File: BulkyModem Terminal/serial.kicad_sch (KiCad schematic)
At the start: 12 parts, among them J2 RS-232, J5 TTL, U2 74HCT244, U3 MAX232

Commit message: Part of a layout
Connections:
- net TTL.CTS: now also J5.3 (Pin_3), R21.2; no longer R21.1, U2.11 (2A3)
- net TTL.RTS: now also J5.4 (Pin_4); no longer U2.5 (2Y1)
- net TTL.RxD: now also J5.1 (Pin_1), R15.2; no longer R15.1, U2.13 (2A2)
- net TTL.TxD: now also J5.2 (Pin_2); no longer U2.3 (2Y0)
- net at R16.2: now also U2.5 (2Y1); no longer J5.4 (Pin_4)
- net at R20.2: now also U2.3 (2Y0); no longer J5.2 (Pin_2)
- new net: R15.1, U2.13 (2A2)
- new net: R21.1, U2.11 (2A3)
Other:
- note added: "CTS"
- note added: "RTS"
- note added: "RxD"
- note added: "TxD"
- moved on the sheet: R15

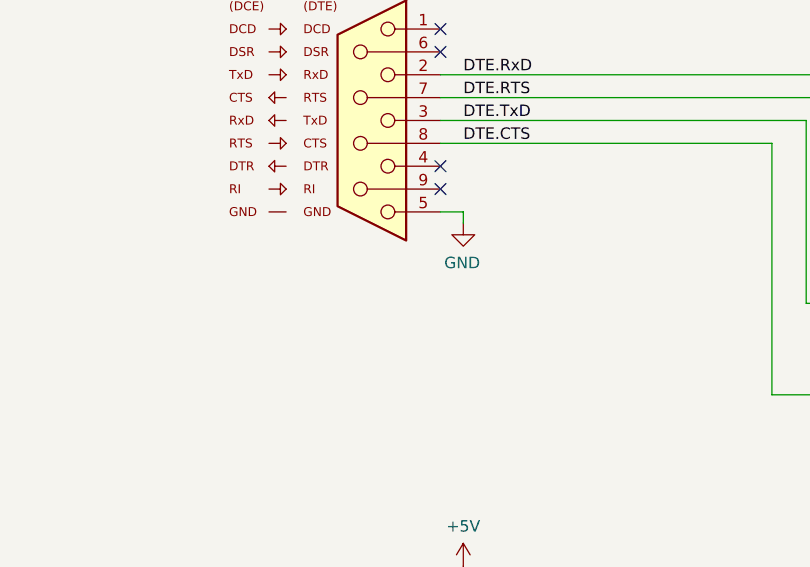
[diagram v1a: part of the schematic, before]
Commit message: Change PS/2 circuit
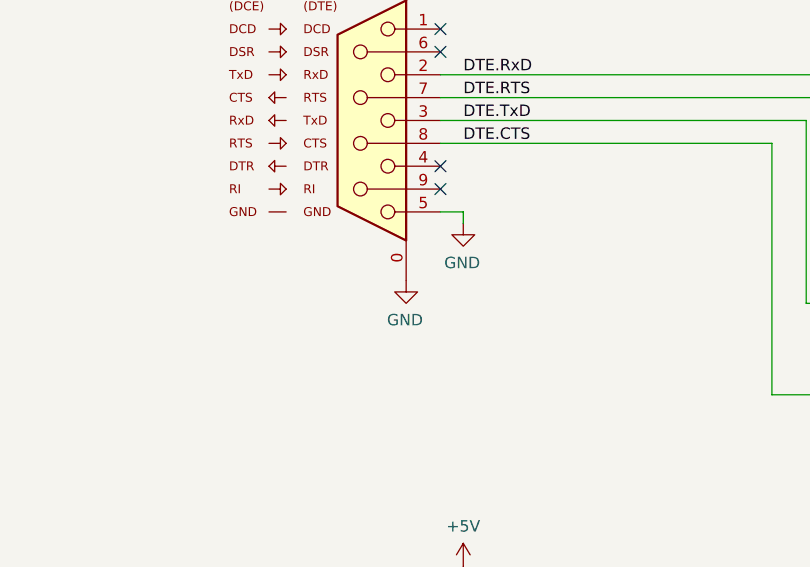
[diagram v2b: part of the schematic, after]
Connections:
- net GND: now also J2.0 (S)
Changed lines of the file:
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@@
 		(pin "2"
+		)
+		(pin "0"
 		)
 		(instances
@@
 					(unit 1)
 				)
+			)
+		)
+	)
+	(symbol
+		(lib_id "power:GND")
+		(at 128.27 102.87 0)
+		(mirror y)
+		(unit 1)
+		(exclude_from_sim no)
+		(in_bom yes)
+		(on_board yes)
+		(dnp no)
+		(property "Reference" "#PWR036"
+			(at 128.27 109.22 0)
+			(effects
+				(font
+					(size 1.27 1.27)
+				)
+				(hide yes)
+			)
+		)
+		(property "Value" "GND"
+			(at 128.143 107.2642 0)
+			(effects
+				(font
+					(size 1.27 1.27)
+				)
+			)
+		)
+		(property "Footprint" ""
+			(at 128.27 102.87 0)
+			(effects
+				(font
+					(size 1.27 1.27)
+				)
+				(hide yes)
+			)
+		)
+		(property "Datasheet" ""
+			(at 128.27 102.87 0)
+			(effects
+				(font
+					(size 1.27 1.27)
+				)
+				(hide yes)
+			)
+		)
+		(property "Description" "Power symbol creates a global label with name \"GND\" , ground"
+			(at 128.27 102.87 0)
+			(effects
+				(font
+					(size 1.27 1.27)
+				)
+				(hide yes)
+			)
+		)
+		(pin "1"
+		)
+		(instances
+			(project "BulkyModem Terminal"
+				(path "/cd9da885-84b5-47eb-b16d-d4099ea4358c/00000000-0000-0000-0000-00006379233a"
+					(reference "#PWR036")
+					(unit 1)
+				)
